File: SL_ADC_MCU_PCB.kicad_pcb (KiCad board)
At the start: 2 copper layers, 1 part, among them IC1 ADS8528SPM

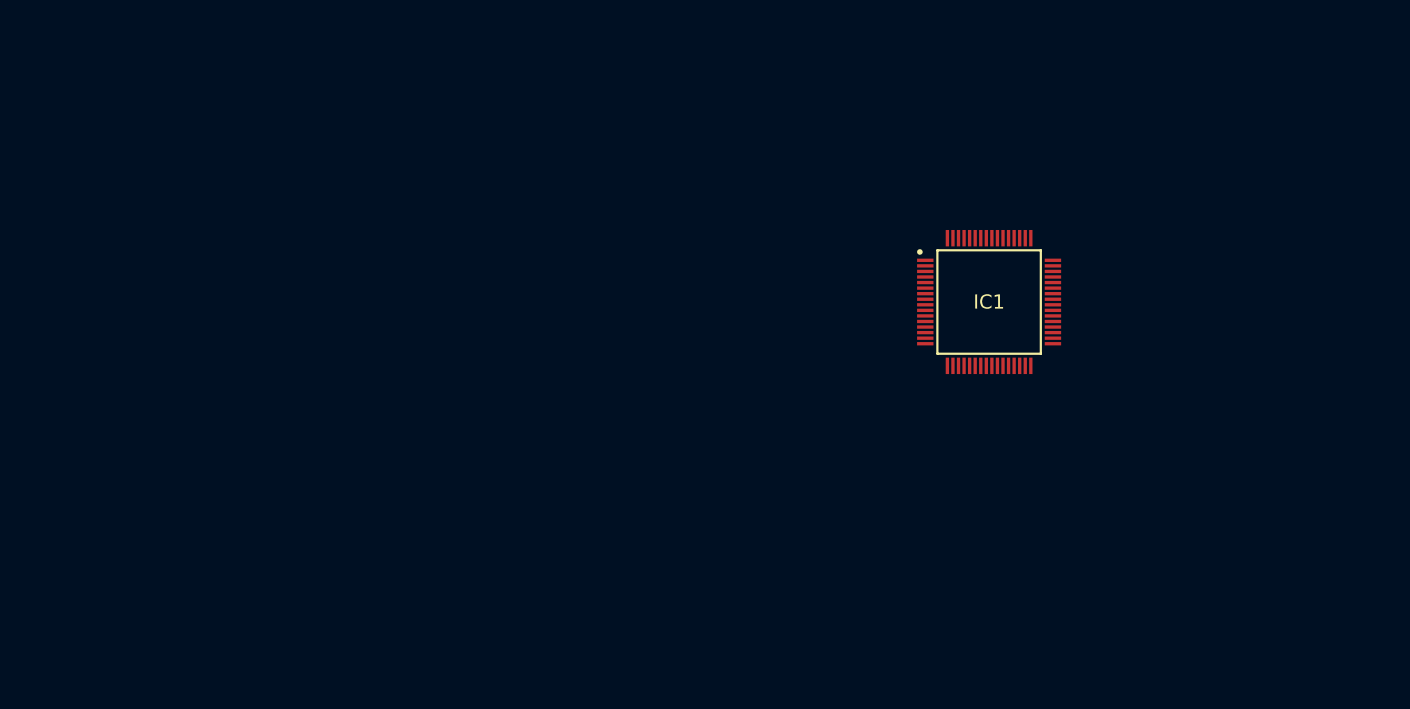
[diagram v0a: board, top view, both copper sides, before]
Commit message: 0-ohm resistor for mcu power and added header for power and hydrophone channels
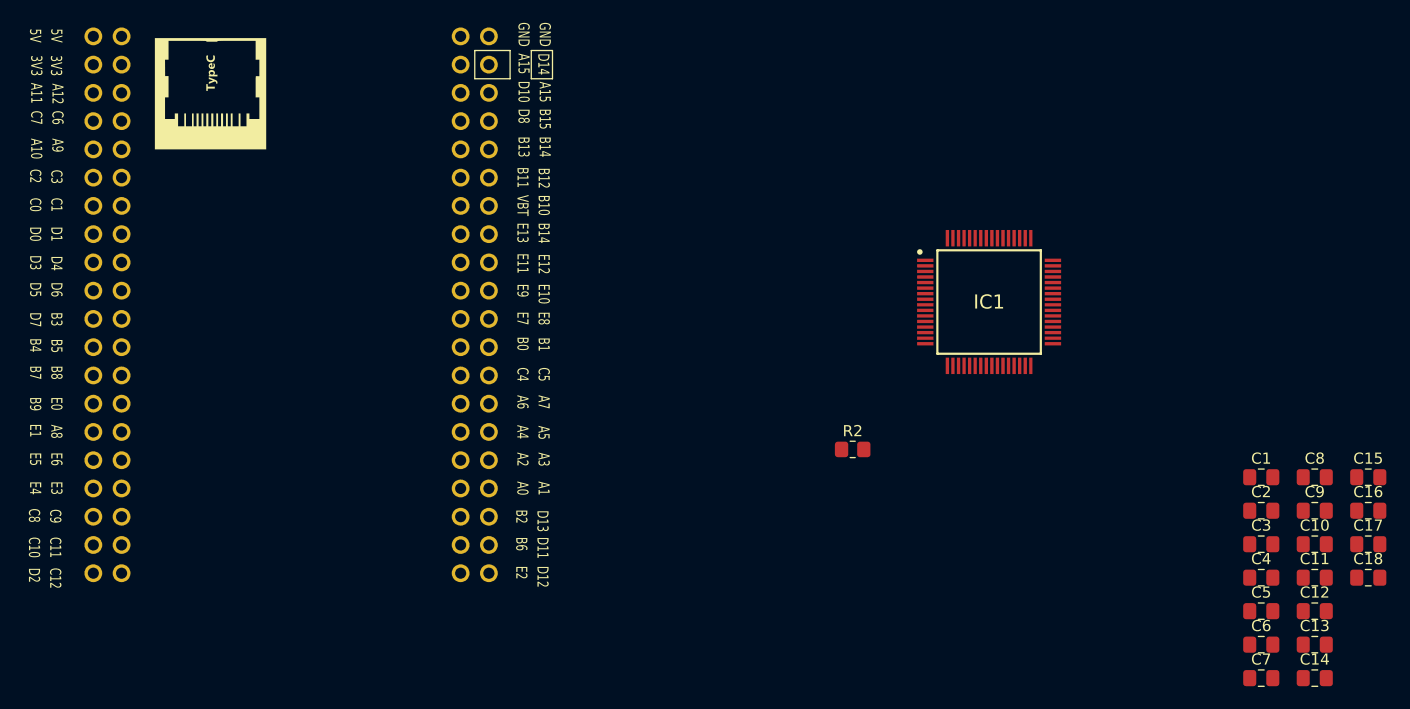
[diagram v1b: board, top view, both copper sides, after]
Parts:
- added C1: 1uF, Capacitor_SMD:C_0805_2012Metric_Pad1.18x1.45mm_HandSolder, F.Cu at (183.7, 85.0)
- added C10: 10uF, Capacitor_SMD:C_0805_2012Metric_Pad1.18x1.45mm_HandSolder, F.Cu at (188.5, 91.0)
- added C11: 10uF, Capacitor_SMD:C_0805_2012Metric_Pad1.18x1.45mm_HandSolder, F.Cu at (188.5, 94.0)
- added C12: 10uF, Capacitor_SMD:C_0805_2012Metric_Pad1.18x1.45mm_HandSolder, F.Cu at (188.5, 97.0)
- added C13: 470nF, Capacitor_SMD:C_0805_2012Metric_Pad1.18x1.45mm_HandSolder, F.Cu at (188.5, 100.0)
- added C14: 10uF, Capacitor_SMD:C_0805_2012Metric_Pad1.18x1.45mm_HandSolder, F.Cu at (188.5, 103.1)
- added C15: 0.1uF, Capacitor_SMD:C_0805_2012Metric_Pad1.18x1.45mm_HandSolder, F.Cu at (193.3, 85.0)
- added C16: 10uF, Capacitor_SMD:C_0805_2012Metric_Pad1.18x1.45mm_HandSolder, F.Cu at (193.3, 88.0)
- added C17: 0.1uF, Capacitor_SMD:C_0805_2012Metric_Pad1.18x1.45mm_HandSolder, F.Cu at (193.3, 91.0)
- added C18: 0.1uF, Capacitor_SMD:C_0805_2012Metric_Pad1.18x1.45mm_HandSolder, F.Cu at (193.3, 94.0)
- added C2: 1uF, Capacitor_SMD:C_0805_2012Metric_Pad1.18x1.45mm_HandSolder, F.Cu at (183.7, 88.0)
- added C3: 1uF, Capacitor_SMD:C_0805_2012Metric_Pad1.18x1.45mm_HandSolder, F.Cu at (183.7, 91.0)
- added C4: 1uF, Capacitor_SMD:C_0805_2012Metric_Pad1.18x1.45mm_HandSolder, F.Cu at (183.7, 94.0)
- added C5: 1uF, Capacitor_SMD:C_0805_2012Metric_Pad1.18x1.45mm_HandSolder, F.Cu at (183.7, 97.0)
- added C6: 1uF, Capacitor_SMD:C_0805_2012Metric_Pad1.18x1.45mm_HandSolder, F.Cu at (183.7, 100.0)
- added C7: 1uF, Capacitor_SMD:C_0805_2012Metric_Pad1.18x1.45mm_HandSolder, F.Cu at (183.7, 103.1)
- added C8: 1uF, Capacitor_SMD:C_0805_2012Metric_Pad1.18x1.45mm_HandSolder, F.Cu at (188.5, 85.0)
- added C9: 10uF, Capacitor_SMD:C_0805_2012Metric_Pad1.18x1.45mm_HandSolder, F.Cu at (188.5, 88.0)
- added R2: 0, Resistor_SMD:R_0805_2012Metric_Pad1.20x1.40mm_HandSolder, F.Cu at (147.0, 82.5)
- added STM1: ~, STM32H7_knockoff:STM32H7_knockoff, F.Cu at (78.7, 45.4)
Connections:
- IC1 pad 1: unconnected-(IC1-HVSS-Pad1) -> /-5V-HVSS
- IC1 pad 10: unconnected-(IC1-RESET-Pad10) -> /RESET
- IC1 pad 11: unconnected-(IC1-REFEN/~{WR}-Pad11) -> /REFEN/~WR
- IC1 pad 12: unconnected-(IC1-~{RD}-Pad12) -> /~RD
- IC1 pad 13: unconnected-(IC1-~{CS}/~{FS}-Pad13) -> /~CS/~FS
- IC1 pad 14: unconnected-(IC1-AVDD_2-Pad14) -> /AVDD
- IC1 pad 15: unconnected-(IC1-AGND_2-Pad15) -> /AGND
- IC1 pad 16: unconnected-(IC1-DB15/SDO_D-Pad16) -> /DB15
- IC1 pad 17: unconnected-(IC1-DB14/SDO_C-Pad17) -> /DB14
- IC1 pad 18: unconnected-(IC1-DB13/SDO_B-Pad18) -> /DB13
- IC1 pad 19: unconnected-(IC1-DB12/SDO_A-Pad19) -> /DB12
- IC1 pad 2: unconnected-(IC1-CH_D1-Pad2) -> /CH_D1
- IC1 pad 20: unconnected-(IC1-DB11/~{REFBUFEN}-Pad20) -> /DB11
- IC1 pad 21: unconnected-(IC1-DB10/SCLK-Pad21) -> /DB10
- IC1 pad 22: unconnected-(IC1-DB9/SDI-Pad22) -> /DB9
- IC1 pad 23: unconnected-(IC1-DB8/DCEN-Pad23) -> /DB8
- IC1 pad 24: unconnected-(IC1-DGND-Pad24) -> /DGND
- IC1 pad 25: unconnected-(IC1-DVDD-Pad25) -> /DVDD
- IC1 pad 26: unconnected-(IC1-DB7-Pad26) -> /DB7
- IC1 pad 27: unconnected-(IC1-DB6/SEL_B-Pad27) -> /DB6
- IC1 pad 28: unconnected-(IC1-DB5/SEL_CD-Pad28) -> /DB5
- IC1 pad 29: unconnected-(IC1-DB4-Pad29) -> /DB4
- IC1 pad 3: unconnected-(IC1-REFDN-Pad3) -> /AGND
- IC1 pad 30: unconnected-(IC1-DB3/DCIN_A-Pad30) -> /DB3
- IC1 pad 31: unconnected-(IC1-DB2/DCIN_B-Pad31) -> /DB2
- IC1 pad 32: unconnected-(IC1-DB1/DCIN_C-Pad32) -> /DB1
- IC1 pad 33: unconnected-(IC1-DB0/DCIN_D-Pad33) -> /DB0
- IC1 pad 34: unconnected-(IC1-RANGE/XCLK-Pad34) -> /RANGE/XCLK
- IC1 pad 35: unconnected-(IC1-BUSY/INT-Pad35) -> /BUSY/INT
- IC1 pad 36: unconnected-(IC1-ASLEEP-Pad36) -> /ASLEEP
- IC1 pad 37: unconnected-(IC1-CONVST_A-Pad37) -> /CONVST_A
- IC1 pad 38: unconnected-(IC1-CONVST_B-Pad38) -> /CONVST_B
- IC1 pad 39: unconnected-(IC1-CONVST_C-Pad39) -> /CONVST_C
- IC1 pad 4: unconnected-(IC1-AVDD_1-Pad4) -> /AVDD
- IC1 pad 40: unconnected-(IC1-CONVST_D-Pad40) -> /CONVST_D
- IC1 pad 41: unconnected-(IC1-~{HW}/SW-Pad41) -> /~HW/SW
- IC1 pad 42: unconnected-(IC1-CH_A0-Pad42) -> /CH_A0
- IC1 pad 43: unconnected-(IC1-REFAP-Pad43) -> /REFAP
- IC1 pad 44: unconnected-(IC1-AGND_3-Pad44) -> /AGND
- IC1 pad 45: unconnected-(IC1-AVDD_3-Pad45) -> /AVDD
- IC1 pad 46: unconnected-(IC1-REFAN-Pad46) -> /AGND
- IC1 pad 47: unconnected-(IC1-CH_A1-Pad47) -> /CH_A1
- IC1 pad 48: unconnected-(IC1-HVDD-Pad48) -> /5V-HVDD
- IC1 pad 49: unconnected-(IC1-CH_B0-Pad49) -> /CH_B0
- IC1 pad 5: unconnected-(IC1-AGND_1-Pad5) -> /AGND
- IC1 pad 50: unconnected-(IC1-REFBP-Pad50) -> /REFBP
- IC1 pad 51: unconnected-(IC1-AGND_4-Pad51) -> /AGND
- IC1 pad 52: unconnected-(IC1-AVDD_4-Pad52) -> /AVDD
- IC1 pad 53: unconnected-(IC1-REFBN-Pad53) -> /AGND
- IC1 pad 54: unconnected-(IC1-CH_B1-Pad54) -> /CH_B1
- IC1 pad 55: unconnected-(IC1-REFN-Pad55) -> /REFN
- IC1 pad 56: unconnected-(IC1-REFIO-Pad56) -> /REFIO
- IC1 pad 57: unconnected-(IC1-AVDD_5-Pad57) -> /AVDD
- IC1 pad 58: unconnected-(IC1-AGND_5-Pad58) -> /AGND
- IC1 pad 59: unconnected-(IC1-CH_C1-Pad59) -> /CH_C1
- IC1 pad 6: unconnected-(IC1-REFDP-Pad6) -> /REFDP
- IC1 pad 60: unconnected-(IC1-REFCN-Pad60) -> /AGND
- IC1 pad 61: unconnected-(IC1-AVDD_6-Pad61) -> /AVDD
- IC1 pad 62: unconnected-(IC1-AGND_6-Pad62) -> /AGND
- IC1 pad 63: unconnected-(IC1-REFCP-Pad63) -> /CH_C1
- IC1 pad 64: unconnected-(IC1-CH_C0-Pad64) -> /CH_C0
- IC1 pad 7: unconnected-(IC1-CH_D0-Pad7) -> /CH_D0
- IC1 pad 8: unconnected-(IC1-~{PAR}/SER-Pad8) -> /~PAR/SER
- IC1 pad 9: unconnected-(IC1-~{STBY}-Pad9) -> /~STBY

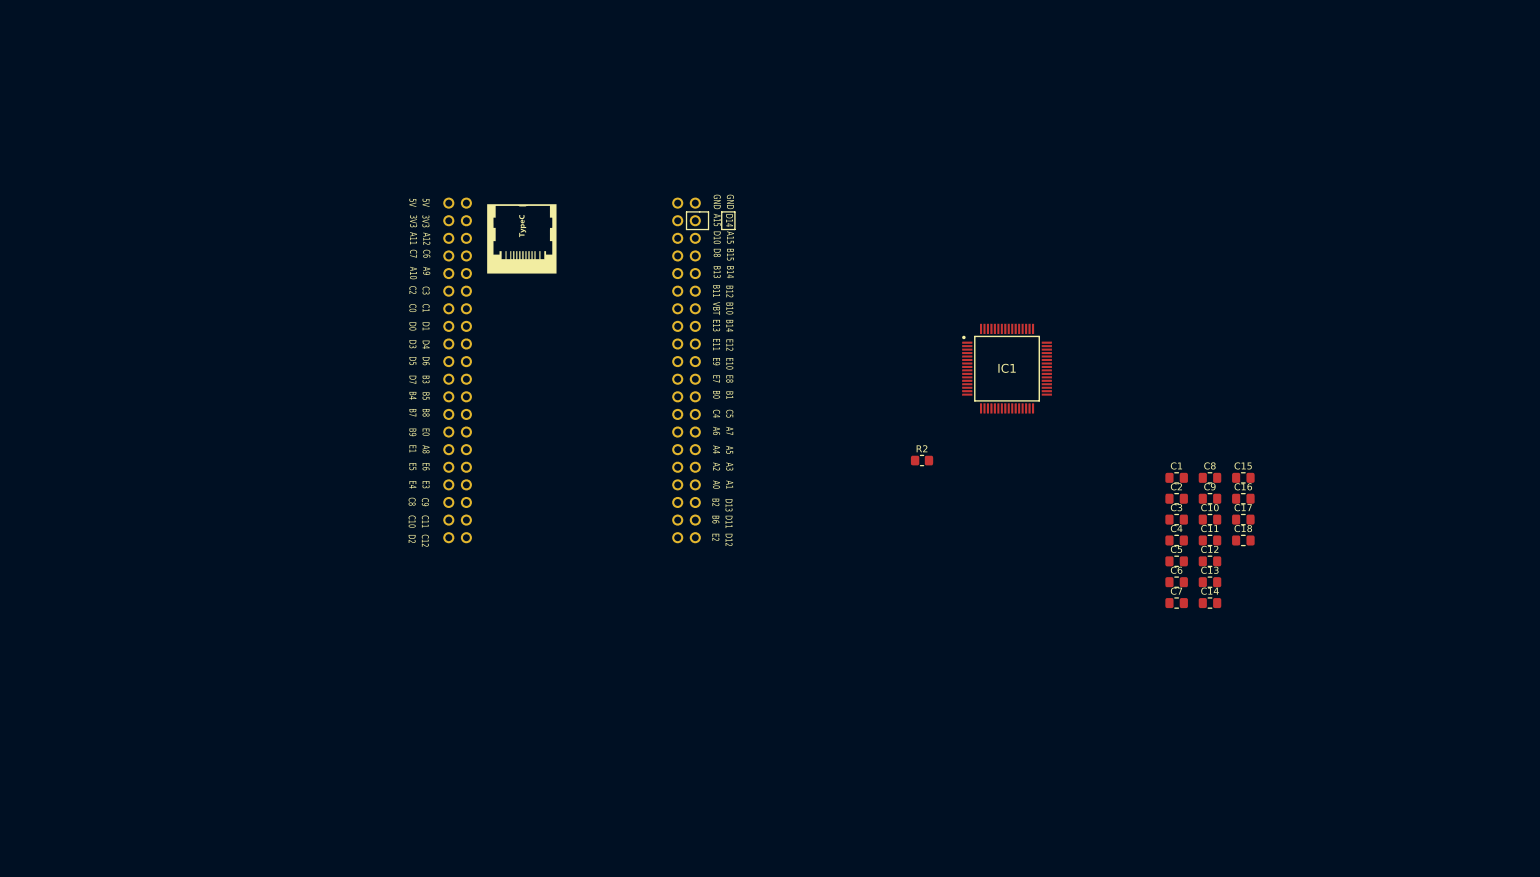
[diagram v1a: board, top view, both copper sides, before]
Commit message: made a few visual edits and added a bunch of testpoints which apparently asks to 'annotate schematic' in the PCB editor, erm...
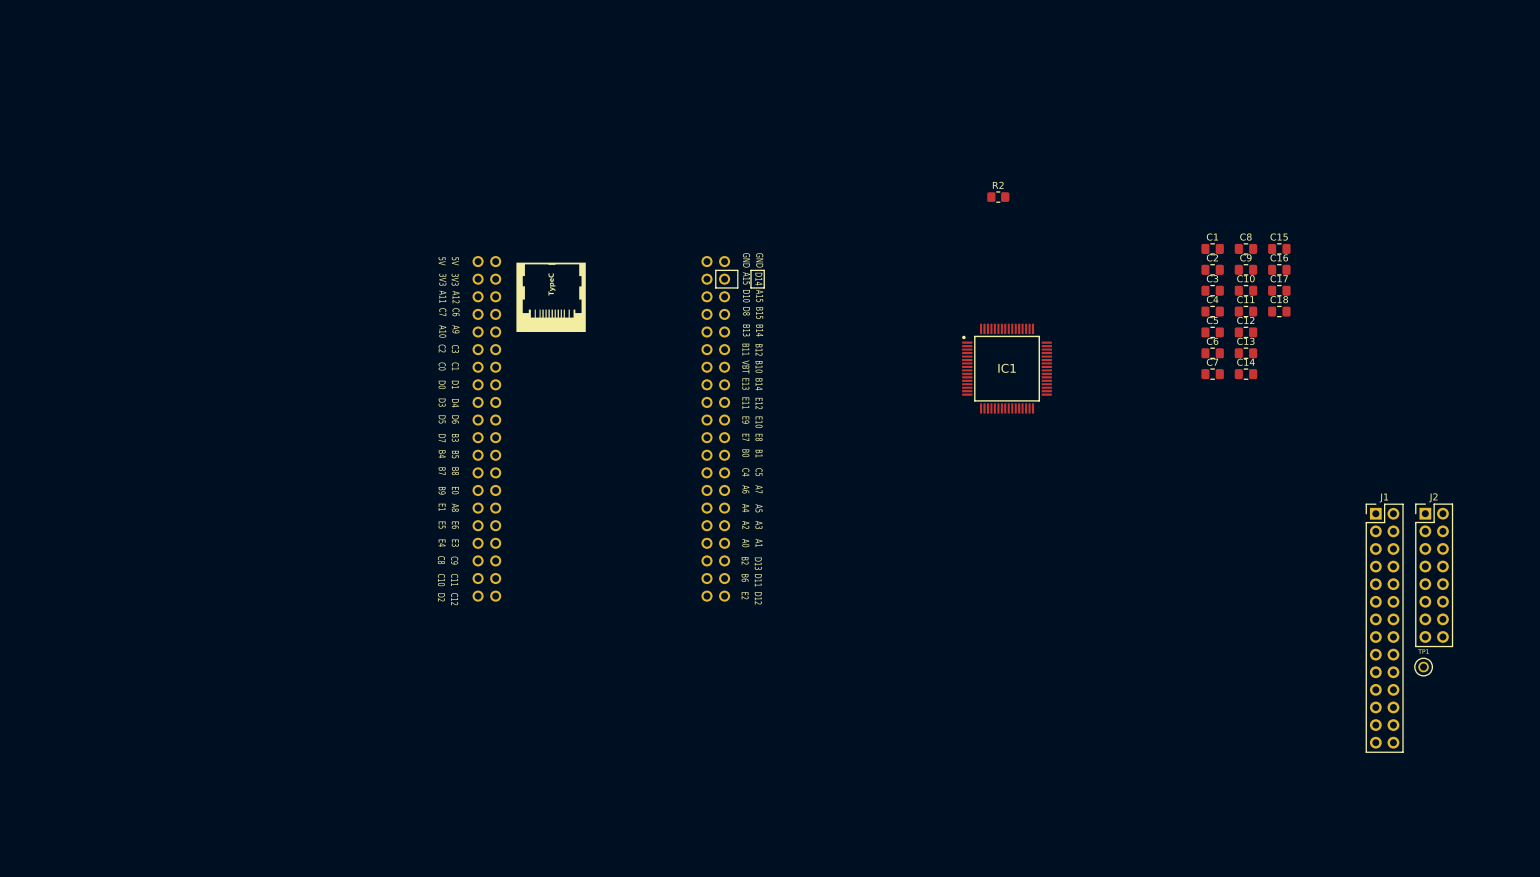
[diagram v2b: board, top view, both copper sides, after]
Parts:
- added J1: Analog header, Connector_PinHeader_2.54mm:PinHeader_2x14_P2.54mm_Vertical, F.Cu at (212.5, 90.2)
- added J2: GPIO breakpoints, Connector_PinHeader_2.54mm:PinHeader_2x08_P2.54mm_Vertical, F.Cu at (219.6, 90.2)
- added TP1: 5117, 5117:KEYSTONE_5117, F.Cu at (219.3, 112.3)
- moved R2 39.6 mm to (158.0, 44.5)
- moved C12 33.4 mm to (193.7, 64.0)
- moved C5 33.4 mm to (188.9, 64.0)
- moved C1 33.4 mm to (188.9, 52.0)
- moved C11 33.4 mm to (193.7, 61.0)
- moved C15 33.4 mm to (198.5, 52.0)
- moved C16 33.4 mm to (198.5, 55.0)
- moved C18 33.4 mm to (198.5, 61.0)
- moved C2 33.4 mm to (188.9, 55.0)
- moved C4 33.4 mm to (188.9, 61.0)
- moved C8 33.4 mm to (193.7, 52.0)
- moved C9 33.4 mm to (193.7, 55.0)
- moved C10 33.4 mm to (193.7, 58.0)
- moved C13 33.4 mm to (193.7, 67.0)
- moved C14 33.4 mm to (193.7, 70.0)
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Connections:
- C18 pad 2: /DGND -> /AGND
- IC1 pad 24: /DGND -> /AGND
- STM1 pad 3V31: unconnected-(STM1-Pad3V31) -> /DVDD
- STM1 pad D0: unconnected-(STM1-PadD0) -> /STM_D0
- STM1 pad D1: unconnected-(STM1-PadD1) -> /STM_D1
- STM1 pad D10: unconnected-(STM1-PadD10) -> /STM_D10
- STM1 pad D3: unconnected-(STM1-PadD3) -> /STM_D3
- STM1 pad D4: unconnected-(STM1-PadD4) -> /STM_D4
- STM1 pad D5: unconnected-(STM1-PadD5) -> /STM_D5
- STM1 pad D6: unconnected-(STM1-PadD6) -> /STM_D6
- STM1 pad D7: unconnected-(STM1-PadD7) -> /STM_D7
- STM1 pad D8: unconnected-(STM1-PadD8) -> /STM_D8
- STM1 pad D9: unconnected-(STM1-PadD9) -> /STM_D9
- STM1 pad E0: unconnected-(STM1-PadE0) -> /STM_E0
- STM1 pad E1: unconnected-(STM1-PadE1) -> /STM_E1
- STM1 pad E3: unconnected-(STM1-PadE3) -> /STM_E3
- STM1 pad E4: unconnected-(STM1-PadE4) -> /STM_E4
- STM1 pad E5: unconnected-(STM1-PadE5) -> /STM_E5
- STM1 pad E6: unconnected-(STM1-PadE6) -> /STM_E6

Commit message: capacitors yet to route, rest done
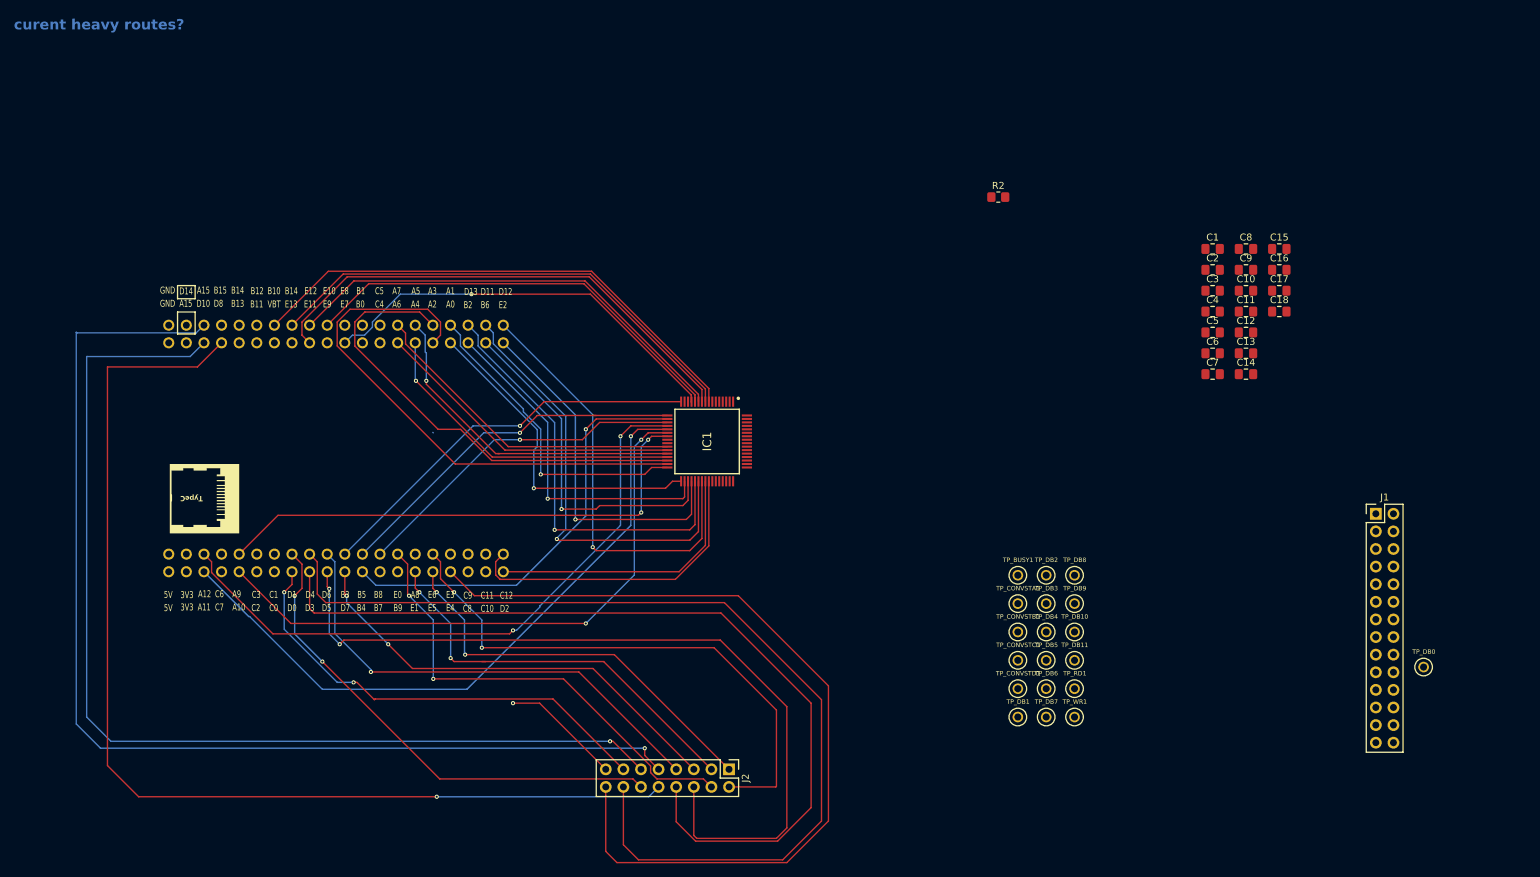
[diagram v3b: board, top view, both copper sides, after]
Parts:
- added TP_BUSY1: 5117, 5117:KEYSTONE_5117, F.Cu at (160.8, 99.0)
- added TP_CONVSTA1: 5117, 5117:KEYSTONE_5117, F.Cu at (160.8, 103.1)
- added TP_CONVSTB1: 5117, 5117:KEYSTONE_5117, F.Cu at (160.8, 107.2)
- added TP_CONVSTC1: 5117, 5117:KEYSTONE_5117, F.Cu at (160.8, 111.3)
- added TP_CONVSTD1: 5117, 5117:KEYSTONE_5117, F.Cu at (160.8, 115.4)
- added TP_DB1: 5117, 5117:KEYSTONE_5117, F.Cu at (160.8, 119.5)
- added TP_DB10: 5117, 5117:KEYSTONE_5117, F.Cu at (169.0, 107.2)
- added TP_DB11: 5117, 5117:KEYSTONE_5117, F.Cu at (169.0, 111.3)
- added TP_DB2: 5117, 5117:KEYSTONE_5117, F.Cu at (164.9, 99.0)
- added TP_DB3: 5117, 5117:KEYSTONE_5117, F.Cu at (164.9, 103.1)
- added TP_DB4: 5117, 5117:KEYSTONE_5117, F.Cu at (164.9, 107.2)
- added TP_DB5: 5117, 5117:KEYSTONE_5117, F.Cu at (164.9, 111.3)
- added TP_DB6: 5117, 5117:KEYSTONE_5117, F.Cu at (164.9, 115.4)
- added TP_DB7: 5117, 5117:KEYSTONE_5117, F.Cu at (164.9, 119.5)
- added TP_DB8: 5117, 5117:KEYSTONE_5117, F.Cu at (169.0, 99.0)
- added TP_DB9: 5117, 5117:KEYSTONE_5117, F.Cu at (169.0, 103.1)
- added TP_RD1: 5117, 5117:KEYSTONE_5117, F.Cu at (169.0, 115.4)
- added TP_WR1: 5117, 5117:KEYSTONE_5117, F.Cu at (169.0, 119.5)
- moved J2 107.0 mm to (119.2, 127.0), turned to -90 degrees
- moved STM1 63.2 mm to (38.3, 98.5), turned to 0 degrees
- moved IC1 44.5 mm to (116.0, 79.8), turned to -90 degrees
- renumbered TP1 to TP_DB0
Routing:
- net /STM_D9: track 0.00 -> 162.7 mm, vias 0 -> 1
- net /STM_D8: track 0.00 -> 157.4 mm, vias 0 -> 1
- net /STM_D10: track 0.00 -> 152.8 mm, vias 0 -> 1
- net /STM_D4: track 0.00 -> 142.9 mm
- net /STM_D3: track 0.00 -> 126.0 mm
- net /STM_E4: track 0.00 -> 125.4 mm
- net /STM_D5: track 0.00 -> 118.6 mm, vias 0 -> 2
- net /DB10: track 0.00 -> 96.9 mm, vias 0 -> 1
- net /DB11: track 0.00 -> 92.6 mm, vias 0 -> 2
- net /DB9: track 0.00 -> 87.1 mm, vias 0 -> 2
- net /STM_E6: track 0.00 -> 80.5 mm, vias 0 -> 2
- net /DB2: track 0.00 -> 78.1 mm
- net /~PAR/SER: track 0.00 -> 74.8 mm
- net /DB8: track 0.00 -> 74.4 mm, vias 0 -> 2
- net /RESET: track 0.00 -> 72.3 mm
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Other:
- board text added: "curent heavy routes?"
